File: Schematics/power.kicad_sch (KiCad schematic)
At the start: 7 parts, among them IC1 LM3940IS-3.3_NOPB

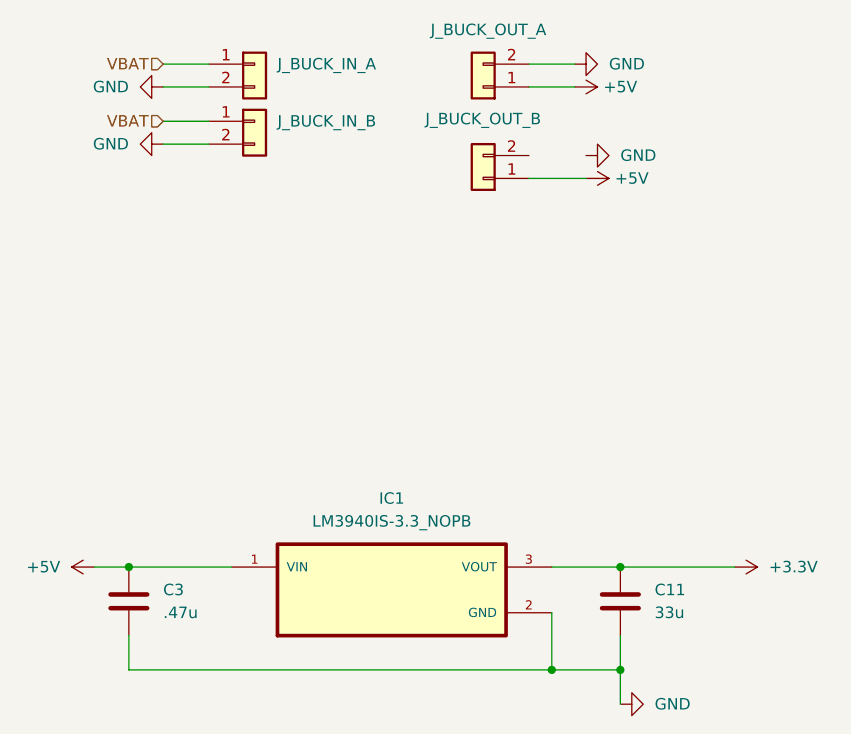
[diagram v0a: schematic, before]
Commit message: assigned footprints ready for pcb design
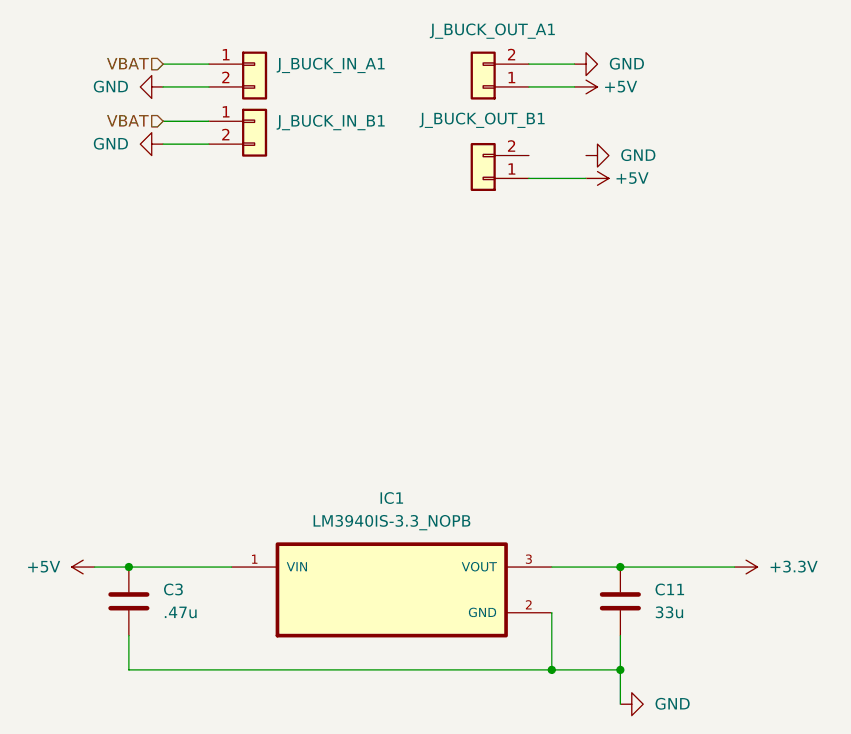
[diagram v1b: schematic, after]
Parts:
- C11, C3: footprint (none) -> Capacitor_SMD:C_0805_2012Metric_Pad1.18x1.45mm_HandSolder
- IC1: footprint TO254P1524X483-4N -> myFootprints:TO254P1524X483-4N
- J_BUCK_IN_A1: renamed from J_BUCK_IN_A; footprint (none) -> Capacitor_SMD:C_0805_2012Metric_Pad1.18x1.45mm_HandSolder
- J_BUCK_IN_B1: renamed from J_BUCK_IN_B; footprint (none) -> Capacitor_SMD:C_0805_2012Metric_Pad1.18x1.45mm_HandSolder
- J_BUCK_OUT_A1: renamed from J_BUCK_OUT_A; footprint (none) -> Capacitor_SMD:C_0805_2012Metric_Pad1.18x1.45mm_HandSolder
- J_BUCK_OUT_B1: renamed from J_BUCK_OUT_B; footprint (none) -> Capacitor_SMD:C_0805_2012Metric_Pad1.18x1.45mm_HandSolder
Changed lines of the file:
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@@
 		(on_board yes)
 		(dnp no)
-		(property "Reference" "J_BUCK_OUT_B"
+		(property "Reference" "J_BUCK_OUT_B1"
 			(at 146.05 45.466 0)
 			(effects
@@
 			)
 		)
-		(property "Footprint" ""
+		(property "Footprint" "Capacitor_SMD:C_0805_2012Metric_Pad1.18x1.45mm_HandSolder"
 			(at 146.05 52.07 0)
 			(effects
@@
 			(project "cameraBoardSchematic"
 				(path "/65068a32-f105-4204-b50e-234054c5a6d0/480e1df8-14aa-40df-bf4b-17bab0b9775f"
-					(reference "J_BUCK_OUT_B")
+					(reference "J_BUCK_OUT_B1")
 					(unit 1)
 				)
@@
 		(dnp no)
 		(fields_autoplaced yes)
-		(property "Reference" "J_BUCK_IN_B"
+		(property "Reference" "J_BUCK_IN_B1"
 			(at 123.19 45.7199 0)
 			(effects
@@
 			)
 		)
-		(property "Footprint" ""
+		(property "Footprint" "Capacitor_SMD:C_0805_2012Metric_Pad1.18x1.45mm_HandSolder"
 			(at 120.65 45.72 0)
 			(effects
@@
 			(project "cameraBoardSchematic"
 				(path "/65068a32-f105-4204-b50e-234054c5a6d0/480e1df8-14aa-40df-bf4b-17bab0b9775f"
-					(reference "J_BUCK_IN_B")
+					(reference "J_BUCK_IN_B1")
 					(unit 1)
 				)
@@
 			)
 		)
-		(property "Footprint" ""
+		(property "Footprint" "Capacitor_SMD:C_0805_2012Metric_Pad1.18x1.45mm_HandSolder"
 			(at 162.2552 102.87 0)
 			(effects
@@
 			)
 		)
-		(property "Footprint" ""
+		(property "Footprint" "Capacitor_SMD:C_0805_2012Metric_Pad1.18x1.45mm_HandSolder"
 			(at 107.6452 102.87 0)
 			(effects
@@
 			)
 		)
-		(property "Footprint" "TO254P1524X483-4N"
+		(property "Footprint" "myFootprints:TO254P1524X483-4N"
 			(at 135.89 97.79 0)
 			(effects
@@
 		(on_board yes)
 		(dnp no)
-		(property "Reference" "J_BUCK_OUT_A"
+		(property "Reference" "J_BUCK_OUT_A1"
 			(at 140.208 35.56 0)
 			(effects
@@
 			)
 		)
-		(property "Footprint" ""
+		(property "Footprint" "Capacitor_SMD:C_0805_2012Metric_Pad1.18x1.45mm_HandSolder"
 			(at 146.05 41.91 0)
 			(effects
@@
 			(project "cameraBoardSchematic"
 				(path "/65068a32-f105-4204-b50e-234054c5a6d0/480e1df8-14aa-40df-bf4b-17bab0b9775f"
-					(reference "J_BUCK_OUT_A")
+					(reference "J_BUCK_OUT_A1")
 					(unit 1)
 				)
@@
 		(dnp no)
 		(fields_autoplaced yes)
-		(property "Reference" "J_BUCK_IN_A"
+		(property "Reference" "J_BUCK_IN_A1"
 			(at 123.19 39.3699 0)
 			(effects
@@
 			)
 		)
-		(property "Footprint" ""
+		(property "Footprint" "Capacitor_SMD:C_0805_2012Metric_Pad1.18x1.45mm_HandSolder"
 			(at 120.65 39.37 0)
 			(effects
@@
 			(project ""
 				(path "/65068a32-f105-4204-b50e-234054c5a6d0/480e1df8-14aa-40df-bf4b-17bab0b9775f"
-					(reference "J_BUCK_IN_A")
-					(unit 1)
-				)
+					(reference "J_BUCK_IN_A1")
+					(unit 1)
+				)

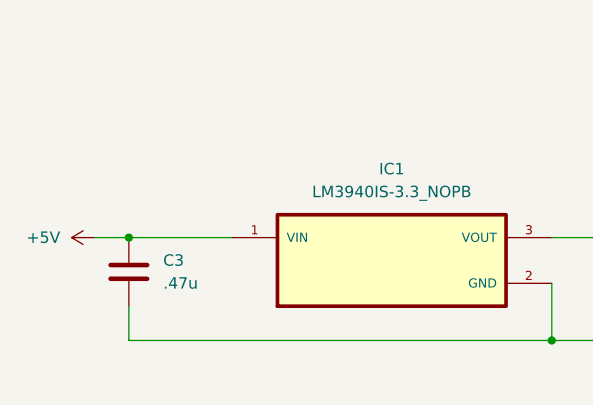
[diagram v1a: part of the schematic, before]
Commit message: Fixed footprint assignments pcb dev begining
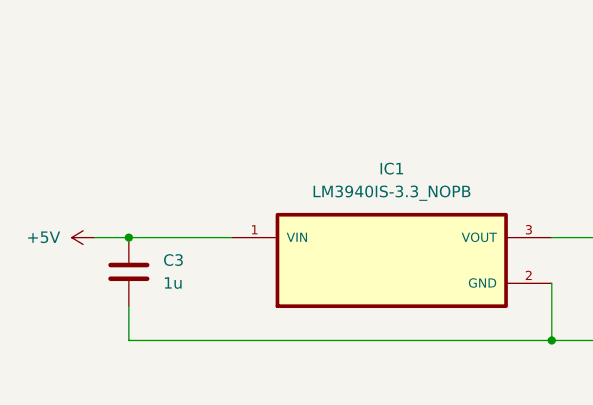
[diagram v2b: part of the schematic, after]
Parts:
- C3: value .47u -> 1u
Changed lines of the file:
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@@
 			)
 		)
-		(property "Value" ".47u"
+		(property "Value" "1u"
 			(at 110.49 100.3299 0)
 			(effects
